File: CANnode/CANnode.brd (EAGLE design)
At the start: 57.9 x 55.2 mm, 247 parts, among them IC1 ISO1050DUB, IC2 ISO1050DUB, Q1 FDV302P, Q3 FDV302P, U1 LM324PW, U10 FT2232HL, U11 93LC56C-I/SN, U2 TPS70445_PWP_24, U3 LM324PW, U4 LM324PW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

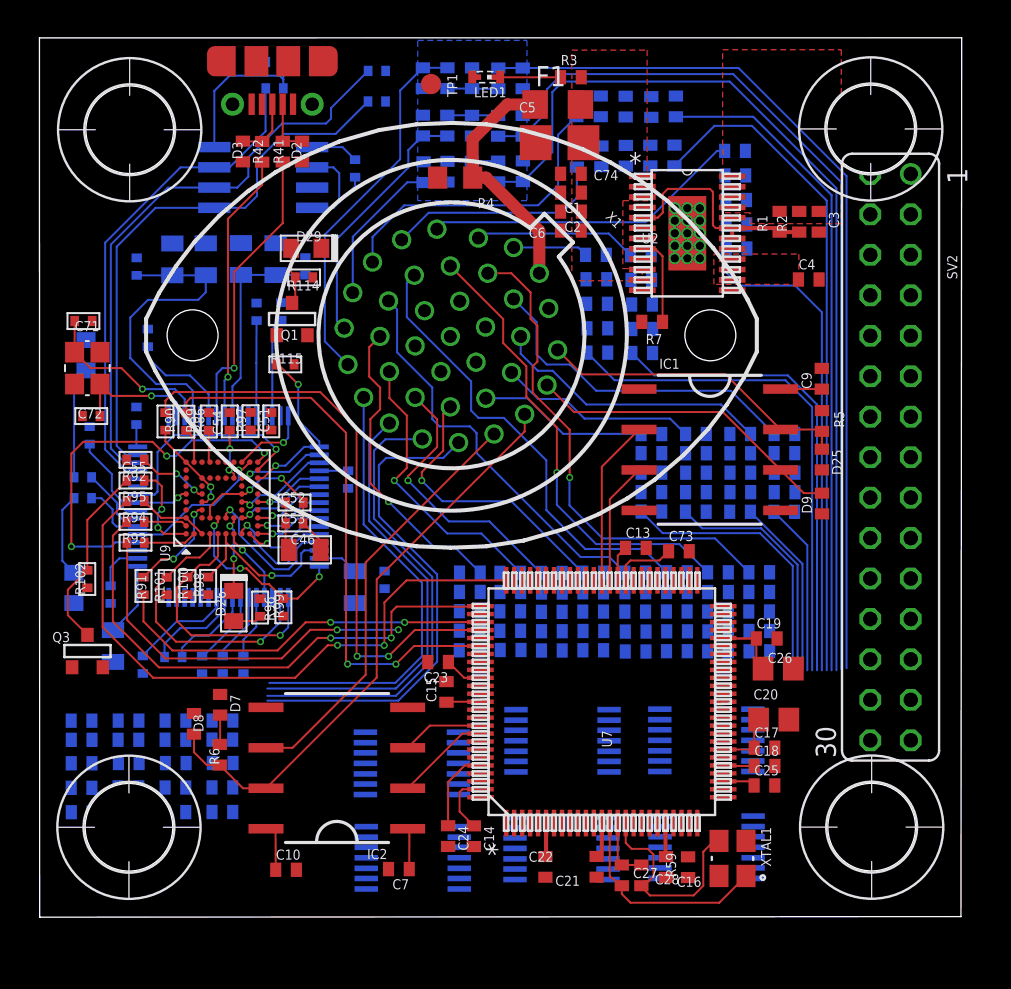
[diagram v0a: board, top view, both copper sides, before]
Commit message: More work on input stages
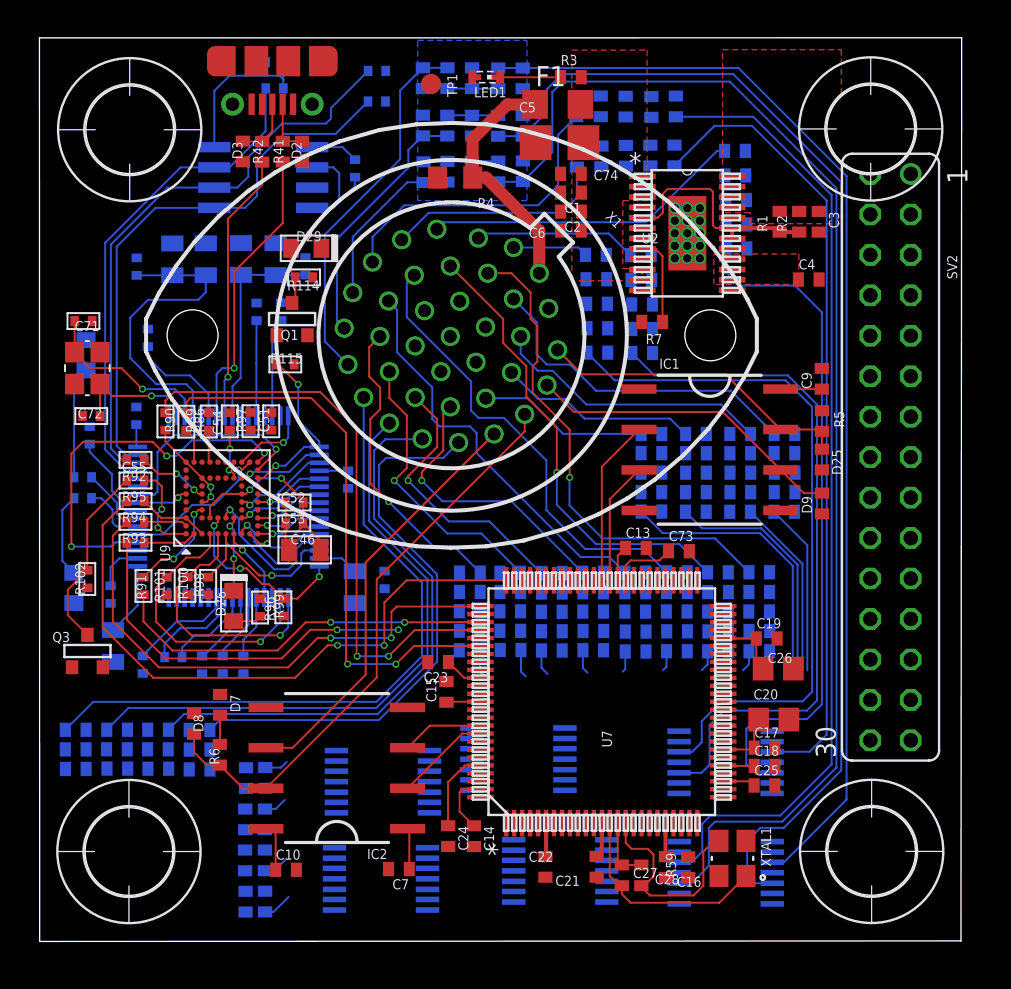
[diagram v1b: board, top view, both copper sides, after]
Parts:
- moved U3 20.5 mm to (29.4, 17.3)
- moved R15 12.8 mm to (22.1, 15.9), turned to 270 degrees
- moved R14 12.5 mm to (20.9, 15.9), turned to 90 degrees
- moved U5 10.3 mm to (51.0, 24.6)
- moved R13 9.09 mm to (22.1, 18.5), turned to 270 degrees
- moved R12 8.64 mm to (20.9, 18.5), turned to 90 degrees
- moved U4 8.40 mm to (51.0, 17.7)
- moved U1 6.69 mm to (38.0, 24.8)
- moved R11 5.64 mm to (22.1, 21.0), turned to 90 degrees
- moved U8 5.13 mm to (29.5, 23.4)
- moved R10 4.82 mm to (20.9, 21.0), turned to 270 degrees
- moved R9 3.44 mm to (22.1, 23.6), turned to 90 degrees
- moved R8 1.59 mm to (20.9, 23.6), turned to 270 degrees
- moved R62 1.56 mm to (18.0, 25.4), turned to 180 degrees
- moved D4 1.56 mm to (18.0, 26.7), turned to 180 degrees
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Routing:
- net A6_3V3: track 59.1 -> 79.5 mm
- net A7_3V3: track 41.6 -> 60.7 mm
- net A5_3V3: track 57.4 -> 75.5 mm
- net A4_3V3: track 55.6 -> 70.1 mm
- net A3_IN: track 28.1 -> 42.1 mm
- net A10_3V3: track 29.7 -> 43.5 mm
- net A11_3V3: track 32.1 -> 44.1 mm
- net A9_3V3: track 31.0 -> 42.6 mm
- net A2_IN: track 27.6 -> 38.7 mm
- net A8_3V3: track 42.0 -> 49.9 mm
- net A1_IN: track 29.3 -> 36.4 mm
- net A0_IN: track 31.1 -> 35.5 mm
- net A3_3V3: track 0.00 -> 1.86 mm
- net D2_3V3: track 0.00 -> 1.78 mm
- net D3_3V3: track 0.00 -> 1.76 mm
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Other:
- board size 57.9 x 55.2 mm -> 57.9 x 56.7 mm

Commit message: Routed buffers
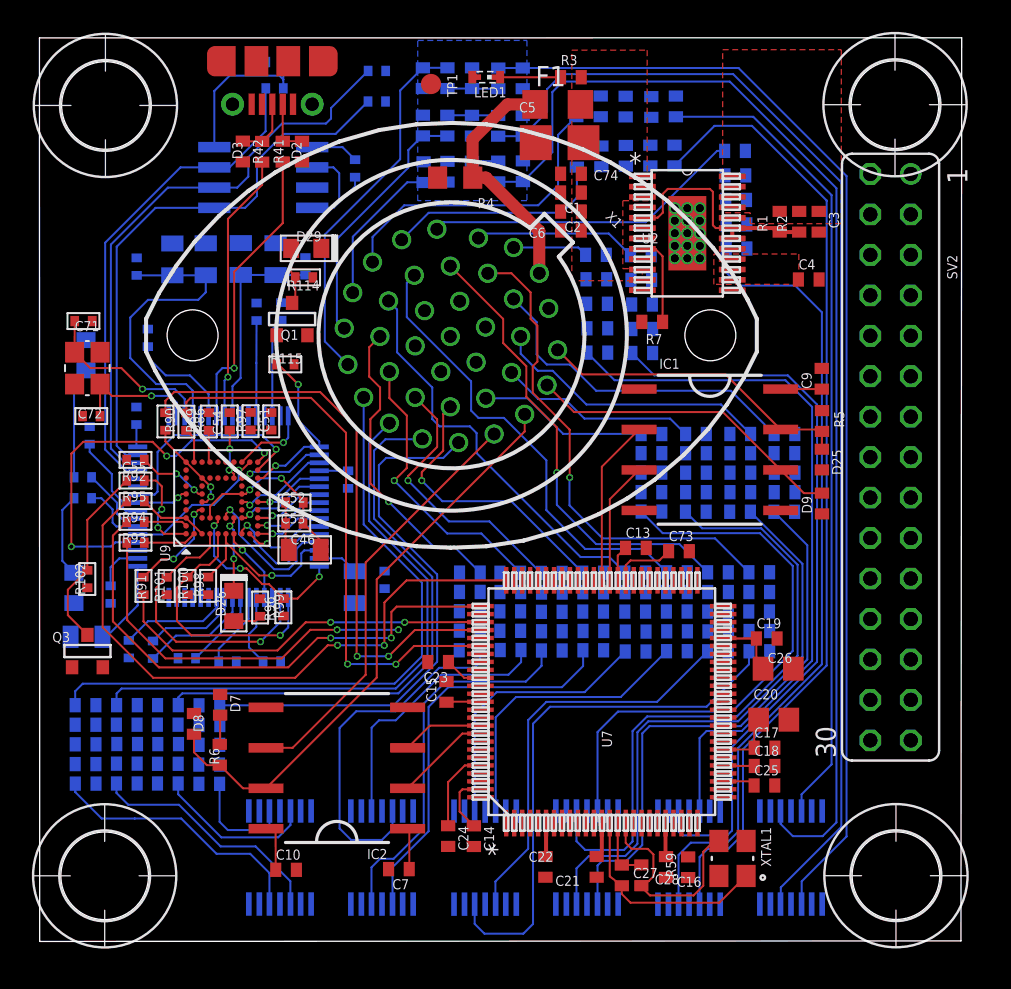
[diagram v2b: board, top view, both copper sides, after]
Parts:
- moved R15 13.5 mm to (10.9, 23.3), turned to 0 degrees
- moved R14 13.2 mm to (10.8, 24.5), turned to 180 degrees
- moved U1 10.6 mm to (29.5, 18.6), turned to 90 degrees
- moved R13 9.93 mm to (13.4, 23.3), turned to 0 degrees
- moved R12 9.59 mm to (13.4, 24.5), turned to 180 degrees
- moved U8 7.99 mm to (35.9, 18.6), turned to 270 degrees
- moved R11 6.50 mm to (16.0, 23.3), turned to 180 degrees
- moved U3 6.48 mm to (23.1, 18.7), turned to 270 degrees
- moved U5 6.41 mm to (48.7, 18.6), turned to 90 degrees
- moved R10 5.98 mm to (16.0, 24.5), turned to 0 degrees
- moved U4 4.21 mm to (55.1, 18.6), turned to 90 degrees
- moved R9 3.54 mm to (18.6, 23.3), turned to 180 degrees
- moved R8 2.47 mm to (18.6, 24.5), turned to 0 degrees
- moved H3 2.16 mm to (61.7, 65.9)
- moved H4 2.16 mm to (12.0, 17.5)
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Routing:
- net D7_3V3: track 1.35 -> 33.9 mm
- net A13_3V3: track 11.3 -> 36.5 mm
- net A12_3V3: track 10.8 -> 35.2 mm
- net A14_3V3: track 15.0 -> 39.2 mm
- net D6_3V3: track 1.35 -> 25.5 mm
- net D0_3V3: track 1.53 -> 25.1 mm
- net D1_3V3: track 1.63 -> 23.8 mm
- net D3_3V3: track 1.76 -> 22.7 mm
- net A15_3V3: track 17.5 -> 35.6 mm
- net D5_3V3: track 1.29 -> 18.3 mm
- net D4_3V3: track 1.32 -> 17.2 mm
- net D2_3V3: track 1.78 -> 17.1 mm
- net A3_3V3: track 1.86 -> 16.8 mm
- net A2_3V3: track 1.64 -> 15.2 mm
- net A8_3V3: track 49.9 -> 60.8 mm
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
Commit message: Finished routing input stages
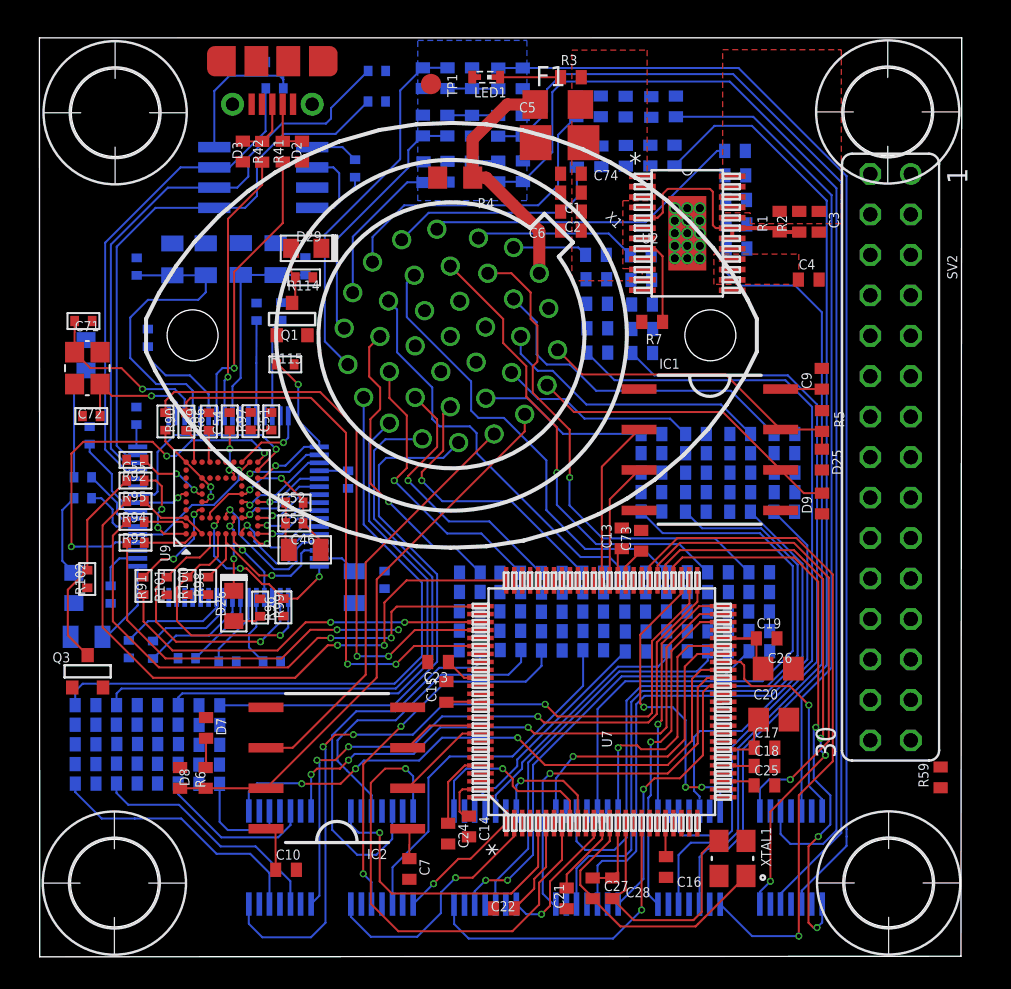
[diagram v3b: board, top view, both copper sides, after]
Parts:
- moved R59 16.8 mm to (64.5, 23.7)
- moved C22 3.69 mm to (37.1, 15.5), turned to 180 degrees
- moved D8 3.51 mm to (16.8, 23.6)
- moved C21 2.73 mm to (41.1, 16.1)
- moved C73 2.46 mm to (45.7, 38.5), turned to 90 degrees
- moved C27 2.00 mm to (42.7, 16.7)
- moved C28 2.00 mm to (43.9, 16.7)
- moved D7 1.70 mm to (18.4, 26.8)
- moved R6 1.70 mm to (18.4, 23.6)
- moved Q3 1.27 mm to (11.0, 30.3)
- moved C13 1.07 mm to (44.5, 38.7), turned to 90 degrees
- moved H4 0.76 mm to (12.7, 17.0)
- moved H2 0.76 mm to (12.7, 65.4)
- moved C14 0.68 mm to (34.9, 20.6)
- moved C7 0.65 mm to (31.2, 17.9), turned to 270 degrees
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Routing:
- net A3_BUFFERED: track 0.00 -> 49.4 mm, vias 0 -> 3
- net A8_BUFFERED: track 0.00 -> 43.4 mm, vias 0 -> 1
- net A2_BUFFERED: track 0.00 -> 41.6 mm, vias 0 -> 3
- net A0_BUFFERED: track 0.00 -> 37.9 mm, vias 0 -> 3
- net A4_BUFFERED: track 0.00 -> 35.6 mm, vias 0 -> 3
- net A1_BUFFERED: track 0.00 -> 35.6 mm, vias 0 -> 3
- net A5_BUFFERED: track 0.00 -> 34.3 mm, vias 0 -> 3
- net D3_BUFFERED: track 0.00 -> 30.7 mm, vias 0 -> 1
- net A6_BUFFERED: track 0.00 -> 30.4 mm, vias 0 -> 1
- net A13_BUFFERED: track 0.00 -> 24.2 mm, vias 0 -> 1
- net A9_BUFFERED: track 0.00 -> 21.1 mm, vias 0 -> 1
- net A11_BUFFERED: track 0.00 -> 19.8 mm, vias 0 -> 3
- net D2_BUFFERED: track 0.00 -> 19.6 mm, vias 0 -> 1
- net D7_BUFFERED: track 0.00 -> 19.6 mm, vias 0 -> 1
- net A14_BUFFERED: track 0.00 -> 18.6 mm, vias 0 -> 1
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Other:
- board size 57.9 x 56.7 mm -> 57.9 x 57.7 mm
